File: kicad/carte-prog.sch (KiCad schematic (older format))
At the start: 14 parts, among them J1 Connecteur côté carte, J2 RJ12 - Côté ordinateur, J3 CHOIX ALIM, J4 DB9_Female, U1 LM1117-3.3, U2 MAX232

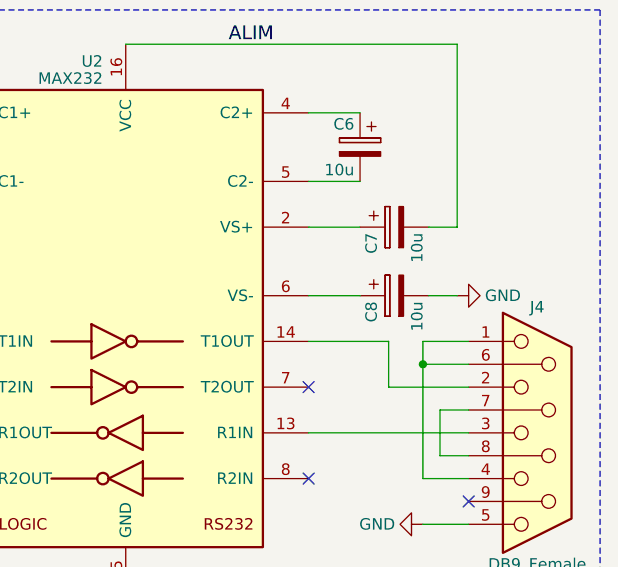
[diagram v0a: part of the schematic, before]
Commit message: Correction sens condensateur V-
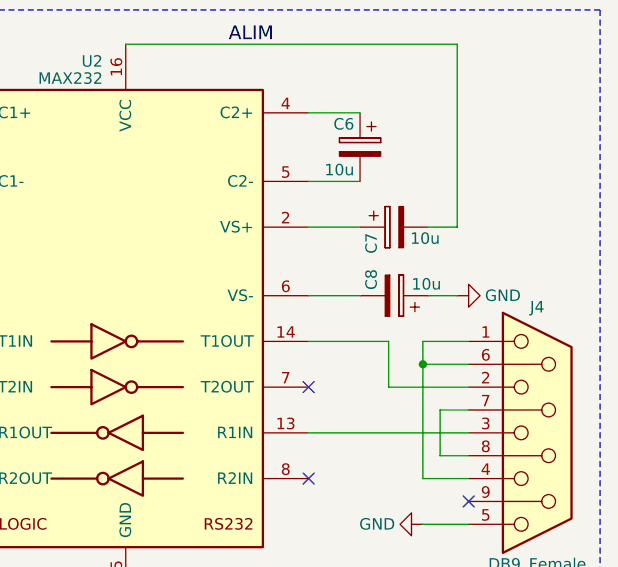
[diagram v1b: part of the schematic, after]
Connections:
- net GND: now also C8.1; no longer C8.2
- net at U2.6 (VS-): now also C8.2; no longer C8.1
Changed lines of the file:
@@
 P 7100 1525
 F 0 "C7" H 7125 1625 50  0000 L CNN
-F 1 "10u" H 7125 1425 50  0000 L CNN
+F 1 "10u" V 7150 1325 50  0000 L CNN
 F 2 "Capacitors_THT:CP_Radial_D5.0mm_P2.50mm" H 7138 1375 50  0001 C CNN
 F 3 "" H 7100 1525 50  0001 C CNN
@@
 U 1 1 5ADA024F
 P 7100 1825
-F 0 "C8" H 7125 1925 50  0000 L CNN
-F 1 "10u" H 7125 1725 50  0000 L CNN
+F 0 "C8" H 7125 1725 50  0000 L CNN
+F 1 "10u" V 7150 1900 50  0000 L CNN
 F 2 "Capacitors_THT:CP_Radial_D5.0mm_P2.50mm" H 7138 1675 50  0001 C CNN
 F 3 "" H 7100 1825 50  0001 C CNN
 	1    7100 1825
-	0    -1   1    0
+	0    1    -1   0
 $EndComp
 $Comp

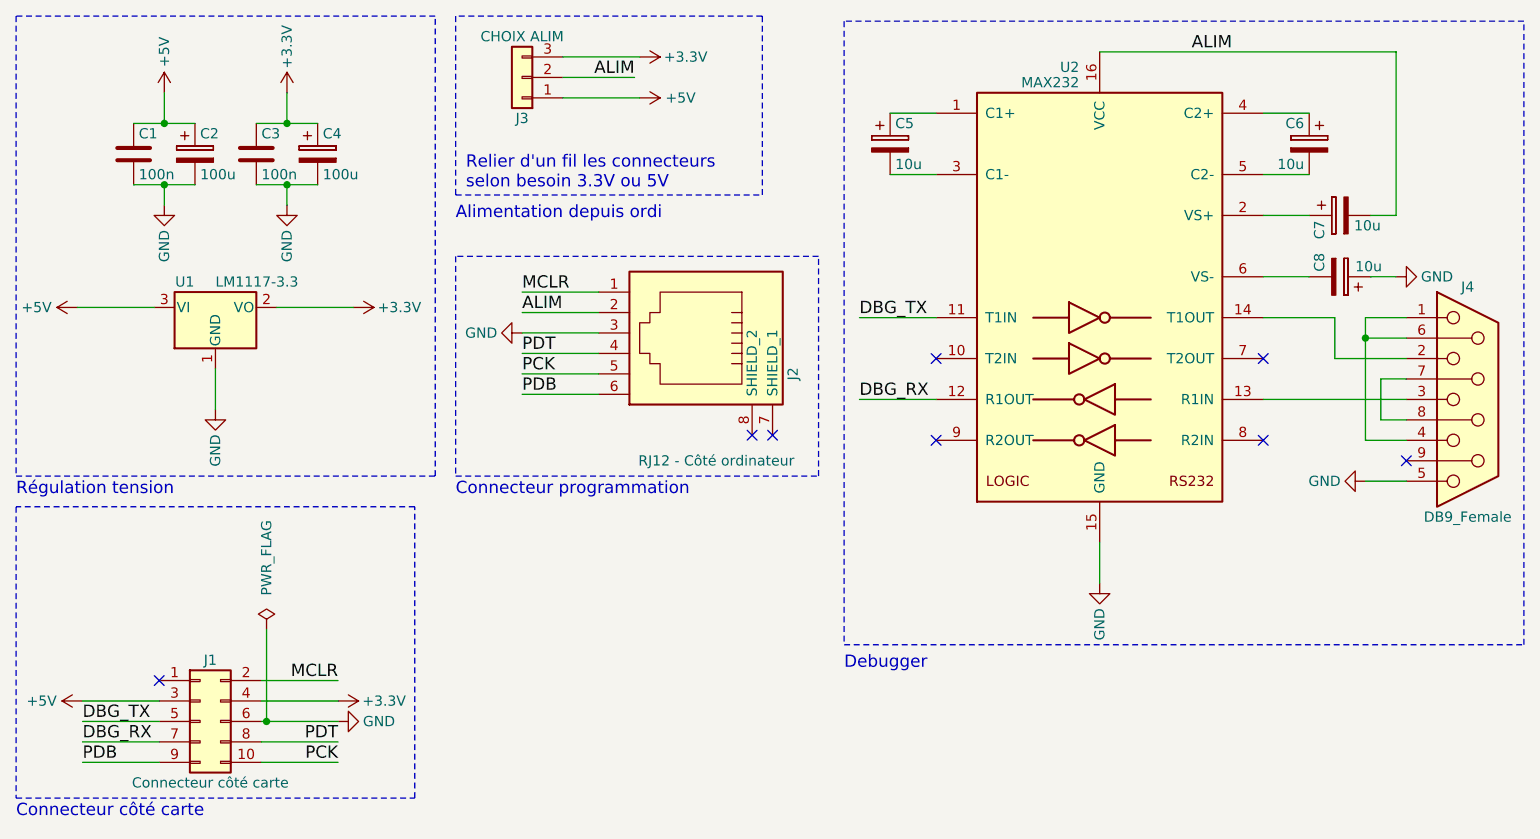
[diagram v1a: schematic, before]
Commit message: Enlèvement connecteur choix alim
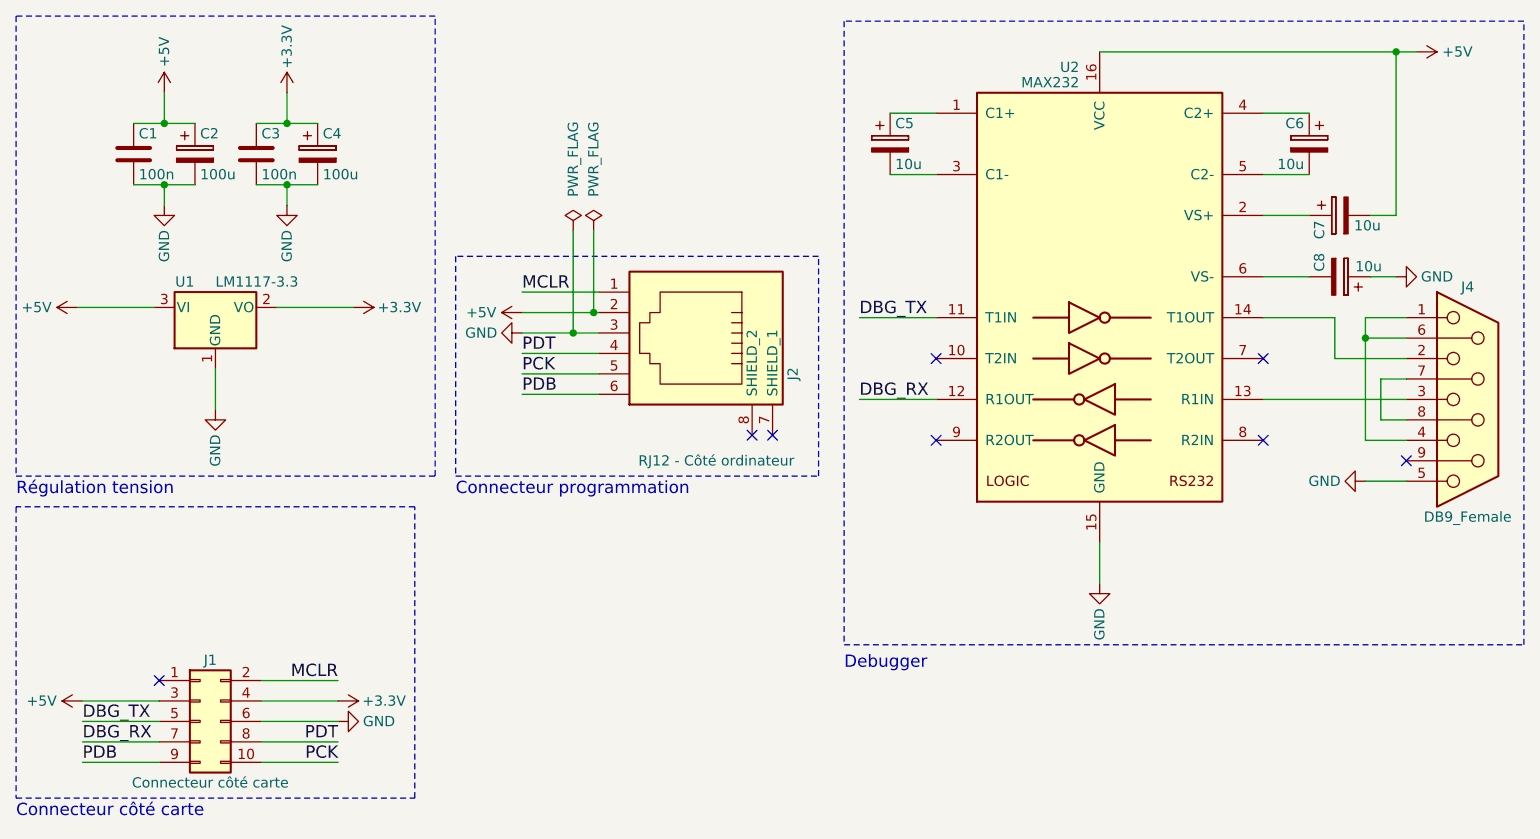
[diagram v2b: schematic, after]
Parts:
- removed J3: CHOIX ALIM, Pin_Headers:Pin_Header_Angled_1x03_Pitch2.54mm, symbol Conn_01x03
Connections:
- net ALIM is gone; now on net +5V: C7.2, J2.2, U2.16 (VCC)
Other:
- note removed: "Alimentation depuis ordi"
- note removed: "Relier d'un fil les connecteurs\nselon besoin 3.3V ou 5V"
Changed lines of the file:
@@
 DBG_TX
-$Comp
-L +3.3V #PWR04
-U 1 1 5ACCB301
-P 3675 750
-F 0 "#PWR04" H 3675 600 50  0001 C CNN
-F 1 "+3.3V" V 3675 975 50  0000 C CNN
-F 2 "" H 3675 750 50  0001 C CNN
-F 3 "" H 3675 750 50  0001 C CNN
-	1    3675 750
-	0    1    1    0
-$EndComp
 $Comp
 L GND #PWR05
@@
 $EndComp
 Wire Wire Line
-	3675 750  3300 750
-Wire Wire Line
 	3100 2100 3475 2100
 Wire Wire Line
@@
 PDB
 Wire Wire Line
-	3675 950  3300 950
-$Comp
-L +5V #PWR06
-U 1 1 5ACCC3AA
-P 3675 950
-F 0 "#PWR06" H 3675 800 50  0001 C CNN
-F 1 "+5V" V 3675 1150 50  0000 C CNN
-F 2 "" H 3675 950 50  0001 C CNN
-F 3 "" H 3675 950 50  0001 C CNN
-	1    3675 950
-	0    1    -1   0
-$EndComp
-Wire Wire Line
 	3100 2000 3475 2000
-Text Label 3100 2000 0    60   ~ 0
-ALIM
-Text Label 3650 850  2    60   ~ 0
-ALIM
-Wire Wire Line
-	3650 850  3300 850
-Text Notes 2825 1400 0    60   ~ 0
-Relier d'un fil les connecteurs\nselon besoin 3.3V ou 5V
-$Comp
-L PWR_FLAG #FLG07
-U 1 1 5ACCC8DD
-P 1850 3550
-F 0 "#FLG07" H 1850 3625 50  0001 C CNN
-F 1 "PWR_FLAG" V 1850 3900 50  0000 C CNN
-F 2 "" H 1850 3550 50  0001 C CNN
-F 3 "" H 1850 3550 50  0001 C CNN
-	1    1850 3550
-	1    0    0    -1
-$EndComp
-Wire Wire Line
-	1850 3550 1850 4000
-Connection ~ 1850 4000
 $Comp
 L MAX232 U2
@@
 	1    7725 2425
 	1    0    0    -1
-$EndComp
-$Comp
-L Conn_01x03 J3
-U 1 1 5AD9DE07
-P 3100 850
-F 0 "J3" H 3100 1050 50  0000 C CNN
-F 1 "CHOIX ALIM" H 3100 650 50  0000 C CNN
-F 2 "Pin_Headers:Pin_Header_Angled_1x03_Pitch2.54mm" H 3100 850 50  0001 C CNN
-F 3 "" H 3100 850 50  0001 C CNN
-	1    3100 850
-	-1   0    0    1
 $EndComp
 Wire Wire Line
@@
 	7375 1525 7250 1525
 Wire Wire Line
-	5925 725  7375 725
+	5925 725  7475 725
 Wire Wire Line
 	7375 725  7375 1525
-Text Label 6375 725  0    60   ~ 0
-ALIM
 NoConn ~ 6725 2625
 NoConn ~ 6725 2225
@@
 Régulation tension
 Wire Notes Line
-	2775 550  2775 1425
-Wire Notes Line
-	2775 1425 4275 1425
-Wire Notes Line
-	4275 1425 4275 550
-Wire Notes Line
-	4275 550  2775 550
-Wire Notes Line
 	4675 3625 8000 3625
 Wire Notes Line
@@
 Wire Notes Line
 	2575 2950 625  2950
-Text Notes 2775 1550 0    60   ~ 0
-Alimentation depuis ordi
 Text Notes 2775 2900 0    60   ~ 0
 Connecteur programmation
@@
 Text Notes 4675 3750 0    60   ~ 0
 Debugger
+$Comp
+L +5V #PWR?
+U 1 1 5ADDF6C7
+P 3100 2000
+F 0 "#PWR?" H 3100 1850 50  0001 C CNN
+F 1 "+5V" V 3100 2200 50  0000 C CNN
+F 2 "" H 3100 2000 50  0001 C CNN
+F 3 "" H 3100 2000 50  0001 C CNN
+	1    3100 2000
+	0    -1   -1   0
+$EndComp
+$Comp
+L +5V #PWR?
+U 1 1 5ADDF747
+P 7475 725
+F 0 "#PWR?" H 7475 575 50  0001 C CNN
+F 1 "+5V" V 7475 925 50  0000 C CNN
+F 2 "" H 7475 725 50  0001 C CNN
+F 3 "" H 7475 725 50  0001 C CNN
+	1    7475 725
+	0    1    1    0
+$EndComp
+Connection ~ 7375 725
+$Comp
+L PWR_FLAG #FLG?
+U 1 1 5ADDFA29
+P 3450 1600
+F 0 "#FLG?" H 3450 1675 50  0001 C CNN
+F 1 "PWR_FLAG" V 3450 1950 50  0000 C CNN
+F 2 "" H 3450 1600 50  0001 C CNN
+F 3 "" H 3450 1600 50  0001 C CNN
+	1    3450 1600
+	1    0    0    -1
+$EndComp
+$Comp
+L PWR_FLAG #FLG?
+U 1 1 5ADDFA5B
+P 3350 1600
+F 0 "#FLG?" H 3350 1675 50  0001 C CNN
+F 1 "PWR_FLAG" V 3350 1950 50  0000 C CNN
+F 2 "" H 3350 1600 50  0001 C CNN
+F 3 "" H 3350 1600 50  0001 C CNN
+	1    3350 1600
+	1    0    0    -1
+$EndComp
+Wire Wire Line
+	3450 1600 3450 2000
+Connection ~ 3450 2000
+Wire Wire Line
+	3350 1600 3350 2100
+Connection ~ 3350 2100
 $EndSCHEMATC
